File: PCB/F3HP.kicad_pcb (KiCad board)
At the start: 2 copper layers, 97 x 107.5 mm, 99 parts, among them J1 L_In, J2 R_In, J3 HPOut, J4 AC_In, J5 Switch, K1 C93402, Q1 BC850C, Q2 BC860C, Q3 BCP56TA, Q4 BC850C, Q5 BC860C, Q6 BCP56TA, Q7 BC850C, Q8 AO3400A, Q9 BC860C, U1 TPS7A4701

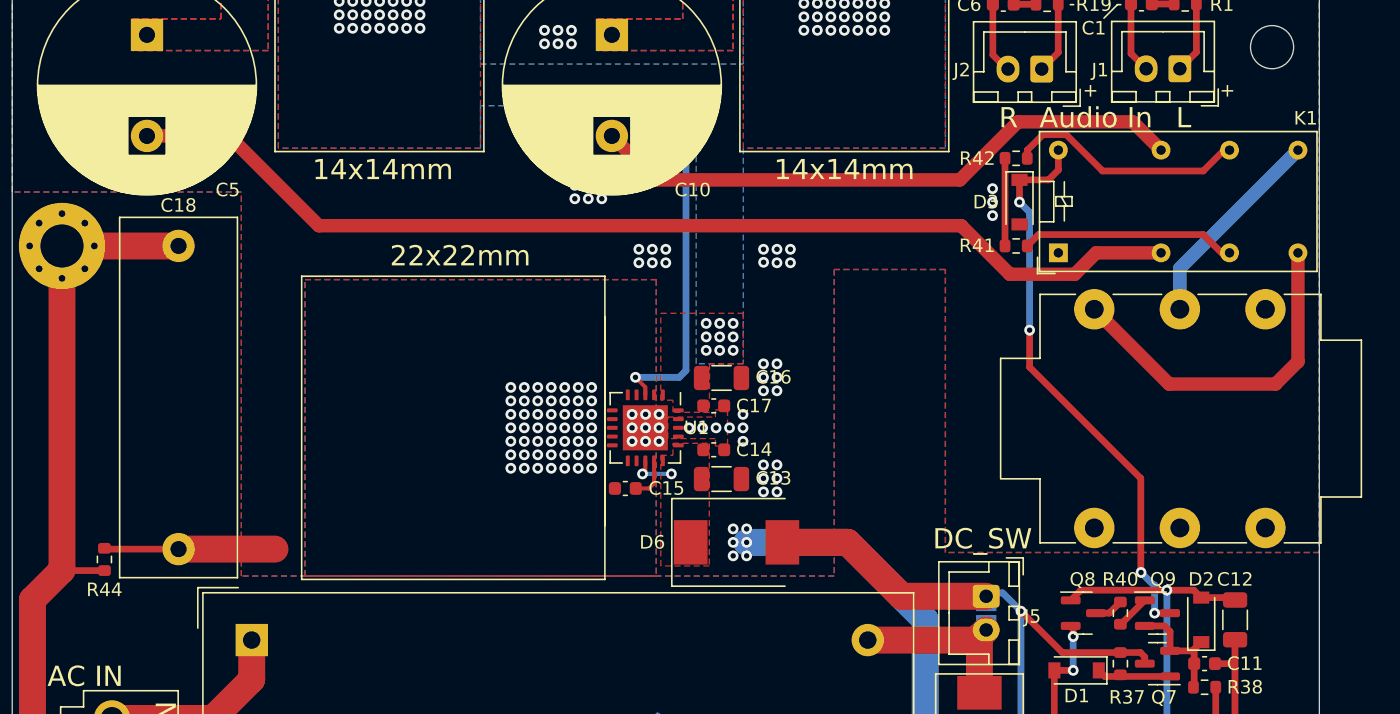
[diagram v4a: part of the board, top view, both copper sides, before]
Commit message: Added back LC filter after ACDC converter
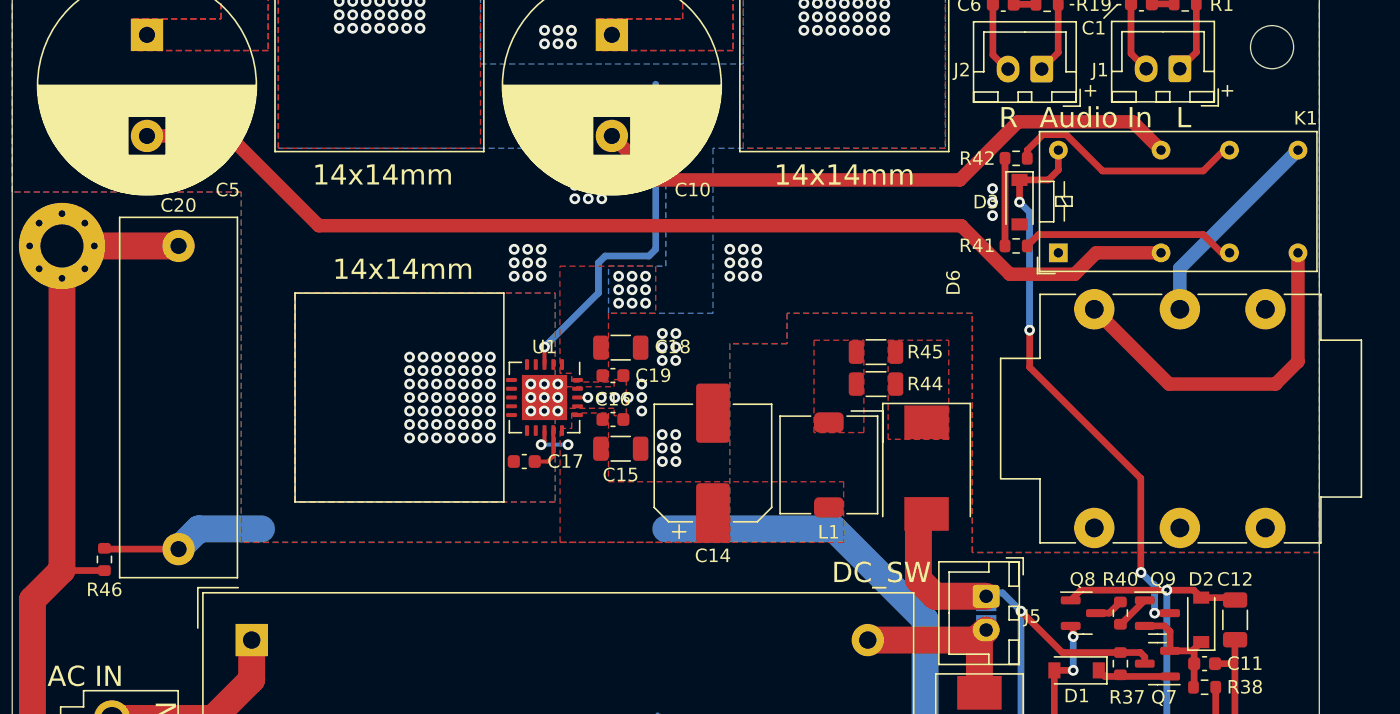
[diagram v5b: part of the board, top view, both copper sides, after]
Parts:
- added C14: 470u, Capacitor_SMD:CP_Elec_8x10.5, F.Cu at (102.0, 90.9)
- added L1: 100u, Inductor_SMD:L_TDK_SLF7032, F.Cu at (110.6, 91.0)
- added R44: 1, Resistor_SMD:R_1206_3216Metric, F.Cu at (114.1, 85.0)
- added R45: 1, Resistor_SMD:R_1206_3216Metric, F.Cu at (114.1, 82.6)
- moved D6 15.1 mm to (117.8, 91.2), turned to -90 degrees
- moved U1 7.81 mm to (89.5, 86.0)
- moved C15 7.81 mm to (95.2, 89.8)
- moved C16 7.81 mm to (94.6, 87.6)
- moved C18 7.81 mm to (95.2, 82.3)
- moved C19 7.81 mm to (94.6, 84.4)
- moved C17 7.76 mm to (88.0, 90.8)
- renumbered C13 to C15, C14 to C16, C15 to C17, C16 to C18, C17 to C19, C18 to C20, R44 to R46
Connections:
- C15 pad 1: Net-(C13-Pad1) -> Net-(C15-Pad1)
- C16 pad 1: Net-(C13-Pad1) -> Net-(C15-Pad1)
- D6 pad 1: Net-(C13-Pad1) -> Net-(D6-Pad1)
- U1 pad 13: Net-(C13-Pad1) -> Net-(C15-Pad1)
- U1 pad 15: Net-(C13-Pad1) -> Net-(C15-Pad1)
- U1 pad 16: Net-(C13-Pad1) -> Net-(C15-Pad1)
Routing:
- net +15V: track 62.9 -> 56.5 mm
- net GND: track 120.4 -> 126.4 mm
- net Net-(C13-Pad1): track 3.20 -> 0.00 mm, vias 2 -> 0
- net Net-(C15-Pad1): track 0.00 -> 3.15 mm, vias 0 -> 2
- added copper zone on F.Cu, net Net-(C15-Pad1)
- added copper zone on F.Cu, net Net-(D6-Pad1)
- added copper zone on F.Cu, net Net-(L1-Pad1)
- removed copper zone on F.Cu, net Net-(C13-Pad1)
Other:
- board text removed: "22x22mm"

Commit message: Added Alps RK163 support
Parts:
- moved RV1 10.0 mm to (147.0, 42.0)
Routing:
- net Net-(C6-Pad2): track 24.1 -> 29.1 mm
- net Net-(C8-Pad1): track 61.1 -> 64.7 mm

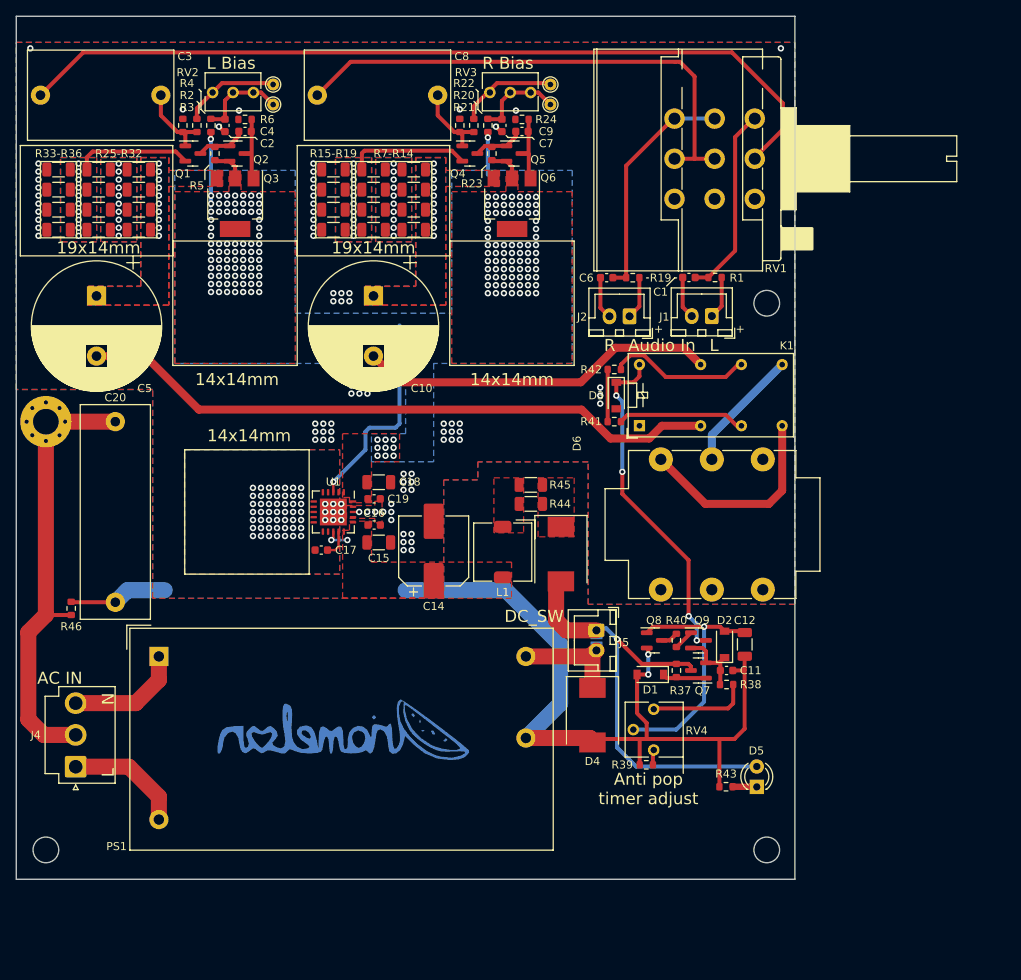
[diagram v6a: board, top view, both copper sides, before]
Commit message: Changed resistors to 1206 to lower distortion
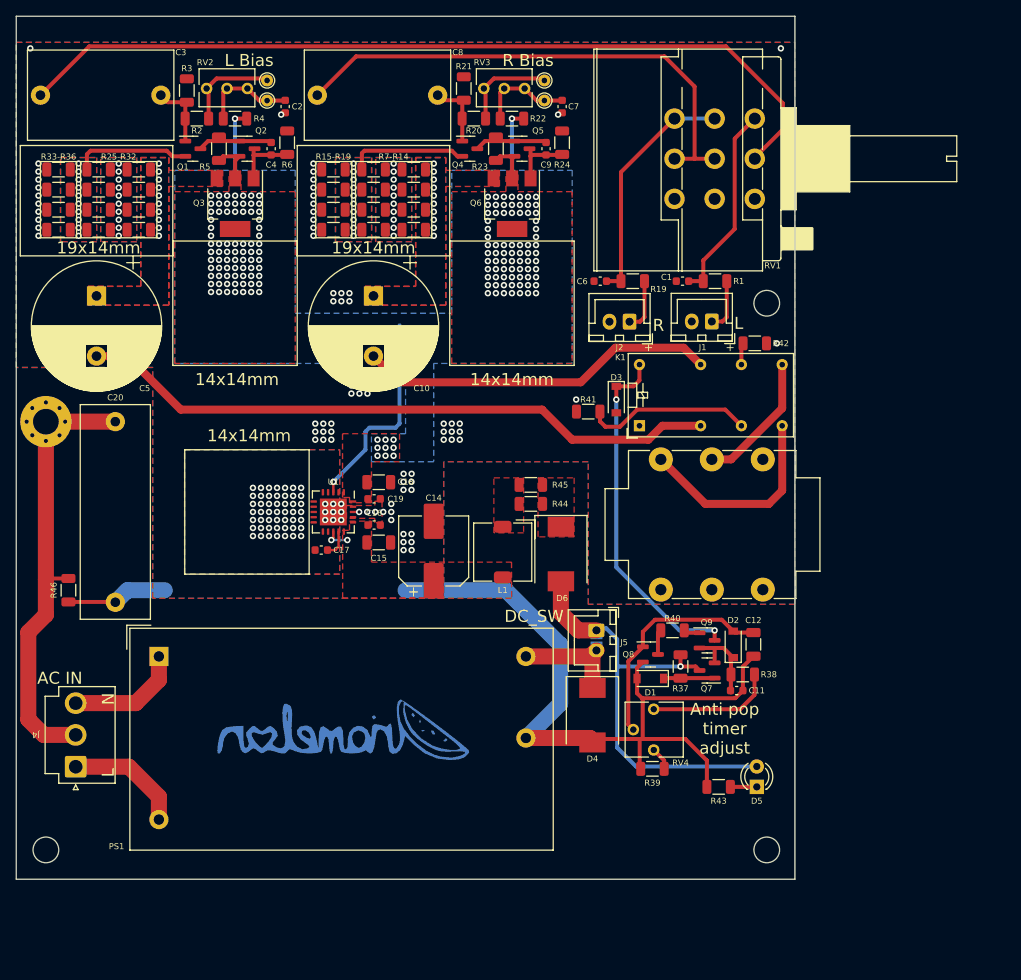
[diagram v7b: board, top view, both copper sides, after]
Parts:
- R1, R19, R2, R20, R21, R22, R23, R24, R3, R37, R38, R39, R4, R40, R41, R42, R43, R46, R5, R6: footprint Resistor_SMD:R_0603_1608Metric -> Resistor_SMD:R_1206_3216Metric
- moved R42 17.8 mm to (142.0, 65.0), turned to 180 degrees
- moved C2 7.86 mm to (83.5, 35.5)
- moved C7 7.86 mm to (118.0, 35.5)
- moved R6 6.00 mm to (83.8, 40.0), turned to 90 degrees
- moved R24 5.78 mm to (118.0, 40.0), turned to 90 degrees
- moved R21 4.63 mm to (105.8, 33.2)
- moved R3 4.38 mm to (71.2, 33.5)
- moved C4 3.90 mm to (81.8, 40.8), turned to 90 degrees
- moved C9 3.69 mm to (116.0, 40.8), turned to 90 degrees
- moved R41 3.48 mm to (121.2, 73.5)
- moved R22 3.12 mm to (111.8, 37.0), turned to 0 degrees
- moved R4 3.12 mm to (77.2, 37.0), turned to 0 degrees
- moved C11 2.80 mm to (139.8, 108.2)
- moved R38 2.37 mm to (140.5, 106.2)
- moved R46 2.29 mm to (56.5, 95.8), turned to 90 degrees
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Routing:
- net GND: track 126.4 -> 105.8 mm, vias 143 -> 136
- net Net-(K1-Pad11): track 17.3 -> 2.44 mm
- net Net-(K1-Pad6): track 15.5 -> 20.8 mm
- net +12V: track 49.8 -> 54.7 mm
- net Net-(C12-Pad1): track 31.8 -> 28.0 mm, vias 1 -> 0
- net Net-(R38-Pad2): track 12.5 -> 15.8 mm
- net Net-(C4-Pad2): track 6.25 -> 9.03 mm
- net Net-(C9-Pad2): track 6.30 -> 8.78 mm
- net Net-(D3-Pad1): track 42.2 -> 44.5 mm, vias 4 -> 2
- net Net-(C8-Pad2): track 9.73 -> 7.52 mm
- net Net-(C11-Pad1): track 8.84 -> 11.0 mm
- net Net-(C3-Pad2): track 9.72 -> 8.25 mm
- net Net-(J3-PadR): track 15.4 -> 16.8 mm
- net Net-(J2-Pad1): track 5.32 -> 6.58 mm
- net Net-(J1-Pad1): track 5.32 -> 6.57 mm
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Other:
- board text removed: "Audio In"
